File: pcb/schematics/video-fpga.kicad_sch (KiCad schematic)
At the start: 8 parts

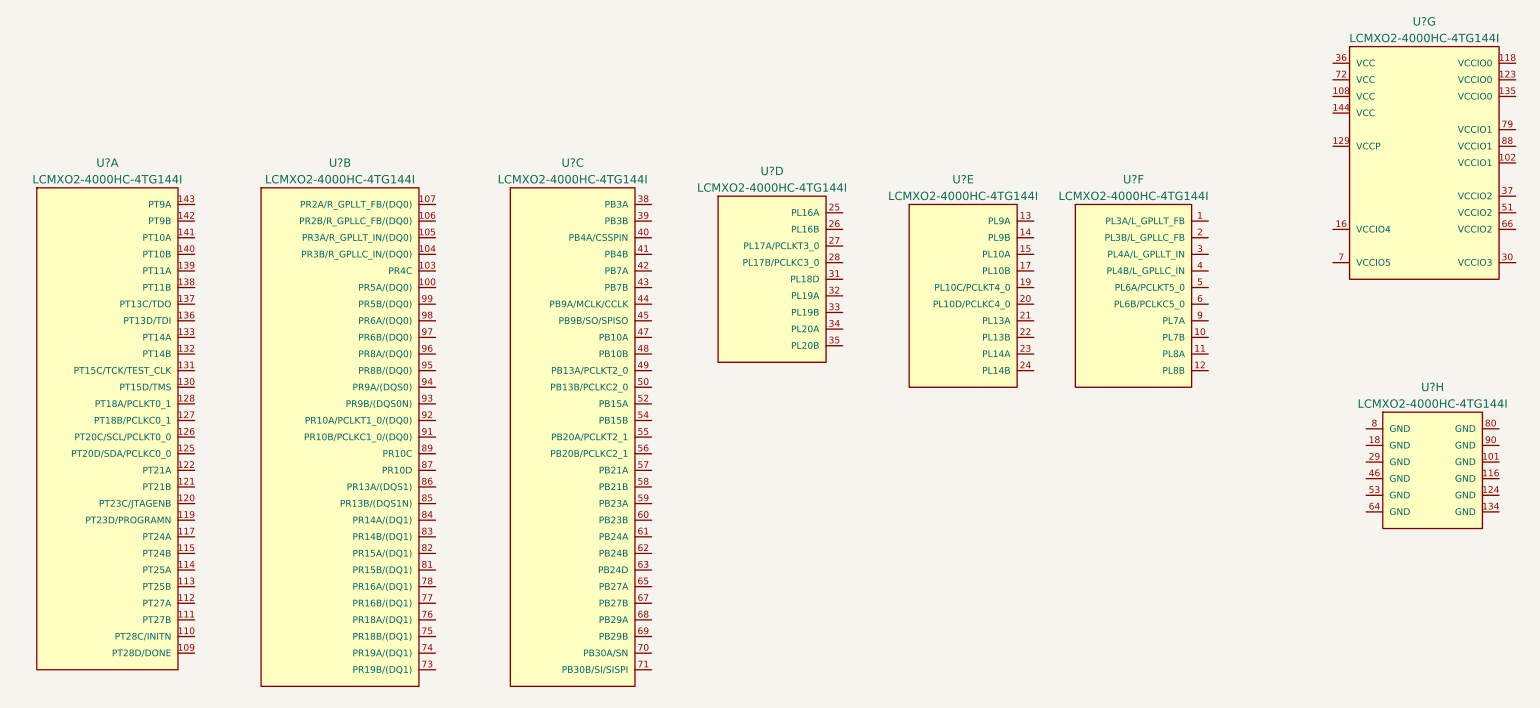
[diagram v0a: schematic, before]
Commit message: change lcmxo2-4000hc for lcmxo2-7000hc to have enough ebr for 1080p text mode
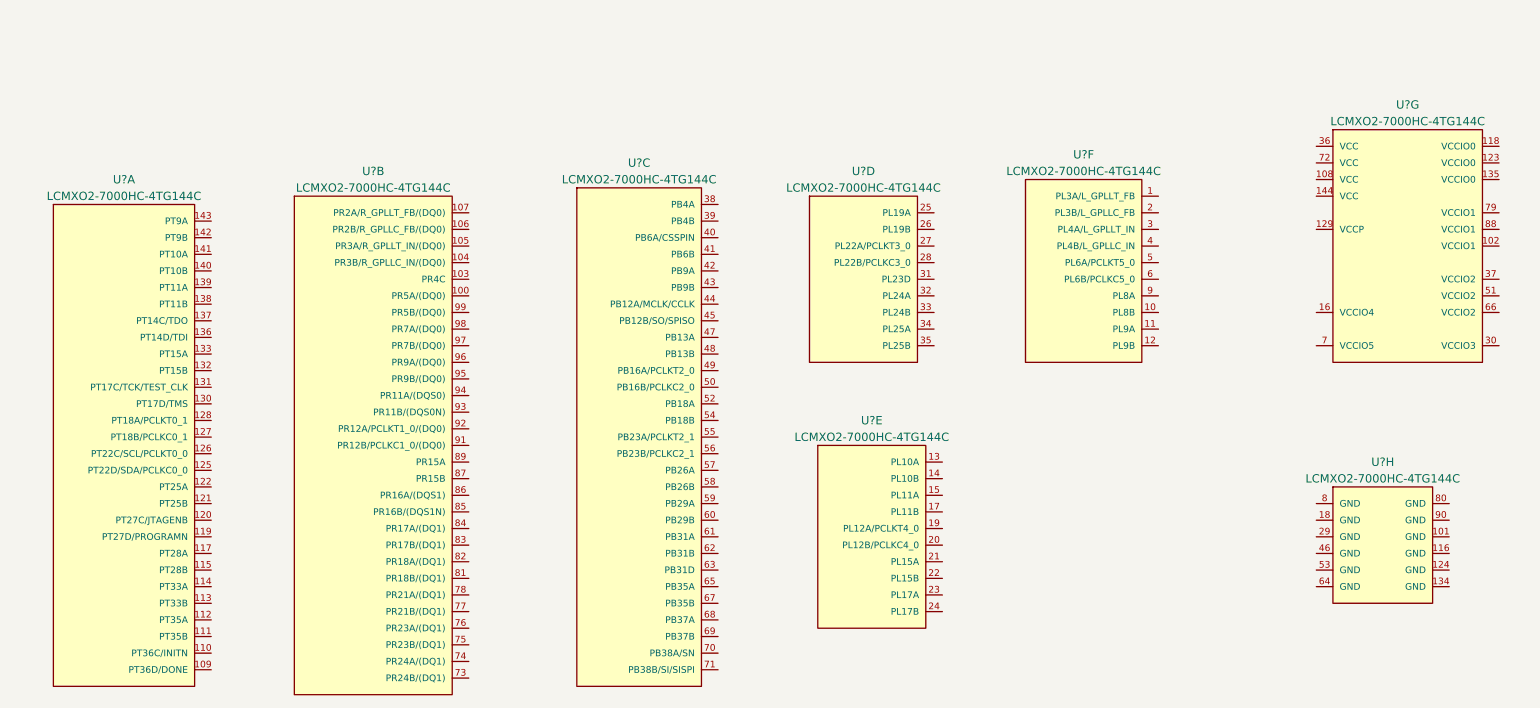
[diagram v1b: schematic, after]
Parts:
- removed U? (x8): LCMXO2-4000HC-4TG144I, Lattice_Semiconductor-LCMXO2-4000HC-4TG144I-*, symbol LCMXO2-4000HC-4TG144I:LCMXO2-4000HC-4TG144I
- added U? (x8): LCMXO2-7000HC-4TG144C, Lattice_Semiconductor-LCMXO2-7000HC-4TG144C-*, symbol LCMXO2-7000HC-4TG144C:LCMXO2-7000HC-4TG144C

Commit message: add bypass to the video controller
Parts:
- added C? (x16): 100n, symbol Device:C_Small
- added C? (x13): 10n, symbol Device:C_Small
- added C? (x7): 1u, symbol Device:C_Small
- added C? (x3): 1n, symbol Device:C_Small
- added D? (x10): D_TVS, symbol Device:D_TVS
- added J? (x2): Conn_01x06, symbol Connector_Generic:Conn_01x06
- added R? (x4): 10k, symbol Device:R_Small
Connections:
- new net +3V3: C?.1, C?.1, C?.1, C?.1, C?.1, C?.1, C?.1, C?.1, C?.1, C?.1, C?.1, C?.1, C?.1, C?.1, C?.1, C?.1, C?.1, C?.1, C?.1, C?.1, C?.1, C?.1, C?.1, C?.1, C?.1, C?.1, C?.1, C?.1, C?.1, C?.1, C?.1, C?.1, C?.1, C?.1, C?.1, C?.1, C?.1, C?.1, C?.1, D?.2 (A2), D?.2 (A2), J?.1 (Pin_1), J?.1 (Pin_1), R?.1, R?.1, R?.1, R?.1, U?.140 (PT10B), U?.141 (PT10A), U?.142 (PT9B), U?.143 (PT9A)
- new net CCK: D?.2 (A2), J?.2 (Pin_2)
- new net GND: C?.2, C?.2, C?.2, C?.2, C?.2, C?.2, C?.2, C?.2, C?.2, C?.2, C?.2, C?.2, C?.2, C?.2, C?.2, C?.2, C?.2, C?.2, C?.2, C?.2, C?.2, C?.2, C?.2, C?.2, C?.2, C?.2, C?.2, C?.2, C?.2, C?.2, C?.2, C?.2, C?.2, C?.2, C?.2, C?.2, C?.2, C?.2, C?.2, D?.1 (A1), D?.1 (A1), D?.1 (A1), D?.1 (A1), D?.1 (A1), D?.1 (A1), D?.1 (A1), D?.1 (A1), D?.1 (A1), D?.1 (A1), J?.6 (Pin_6), J?.6 (Pin_6), U?.138 (PT11B), U?.139 (PT11A), U?.140 (PT10B), U?.141 (PT10A), U?.142 (PT9B), U?.143 (PT9A)
- new net MISO: D?.2 (A2), J?.4 (Pin_4)
- new net MOSI: D?.2 (A2), J?.3 (Pin_3)
- new net SN: D?.2 (A2), J?.5 (Pin_5), R?.2
- new net TCK: D?.2 (A2), J?.2 (Pin_2)
- new net TDI: D?.2 (A2), J?.3 (Pin_3), R?.2
- new net TDO: D?.2 (A2), J?.4 (Pin_4), R?.2
- new net TMS: D?.2 (A2), J?.5 (Pin_5), R?.2
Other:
- note added: "JTAG connector"
- note added: "SPI connector"
- moved on the sheet: U?A

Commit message: add jtag signals to the video controller
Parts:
- added C?: 100p, symbol Device:C_Small
- added R?: 10k, symbol Device:R_Small
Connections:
- net CCK: now also U?.137 (PT14C/TDO)
- net GND: now also C?.2
- net MISO: now also U?.136 (PT14D/TDI)
- net SN: now also U?.109 (PT36D/DONE)
- net TCK: now also U?.131 (PT17C/TCK/TEST_CLK), R?.1
- net TDI: now also U?.136 (PT14D/TDI)
- net TDO: now also U?.137 (PT14C/TDO)
- net TMS: now also U?.130 (PT17D/TMS)
- new net: C?.1, R?.2
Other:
- moved on the sheet: D?, U?A

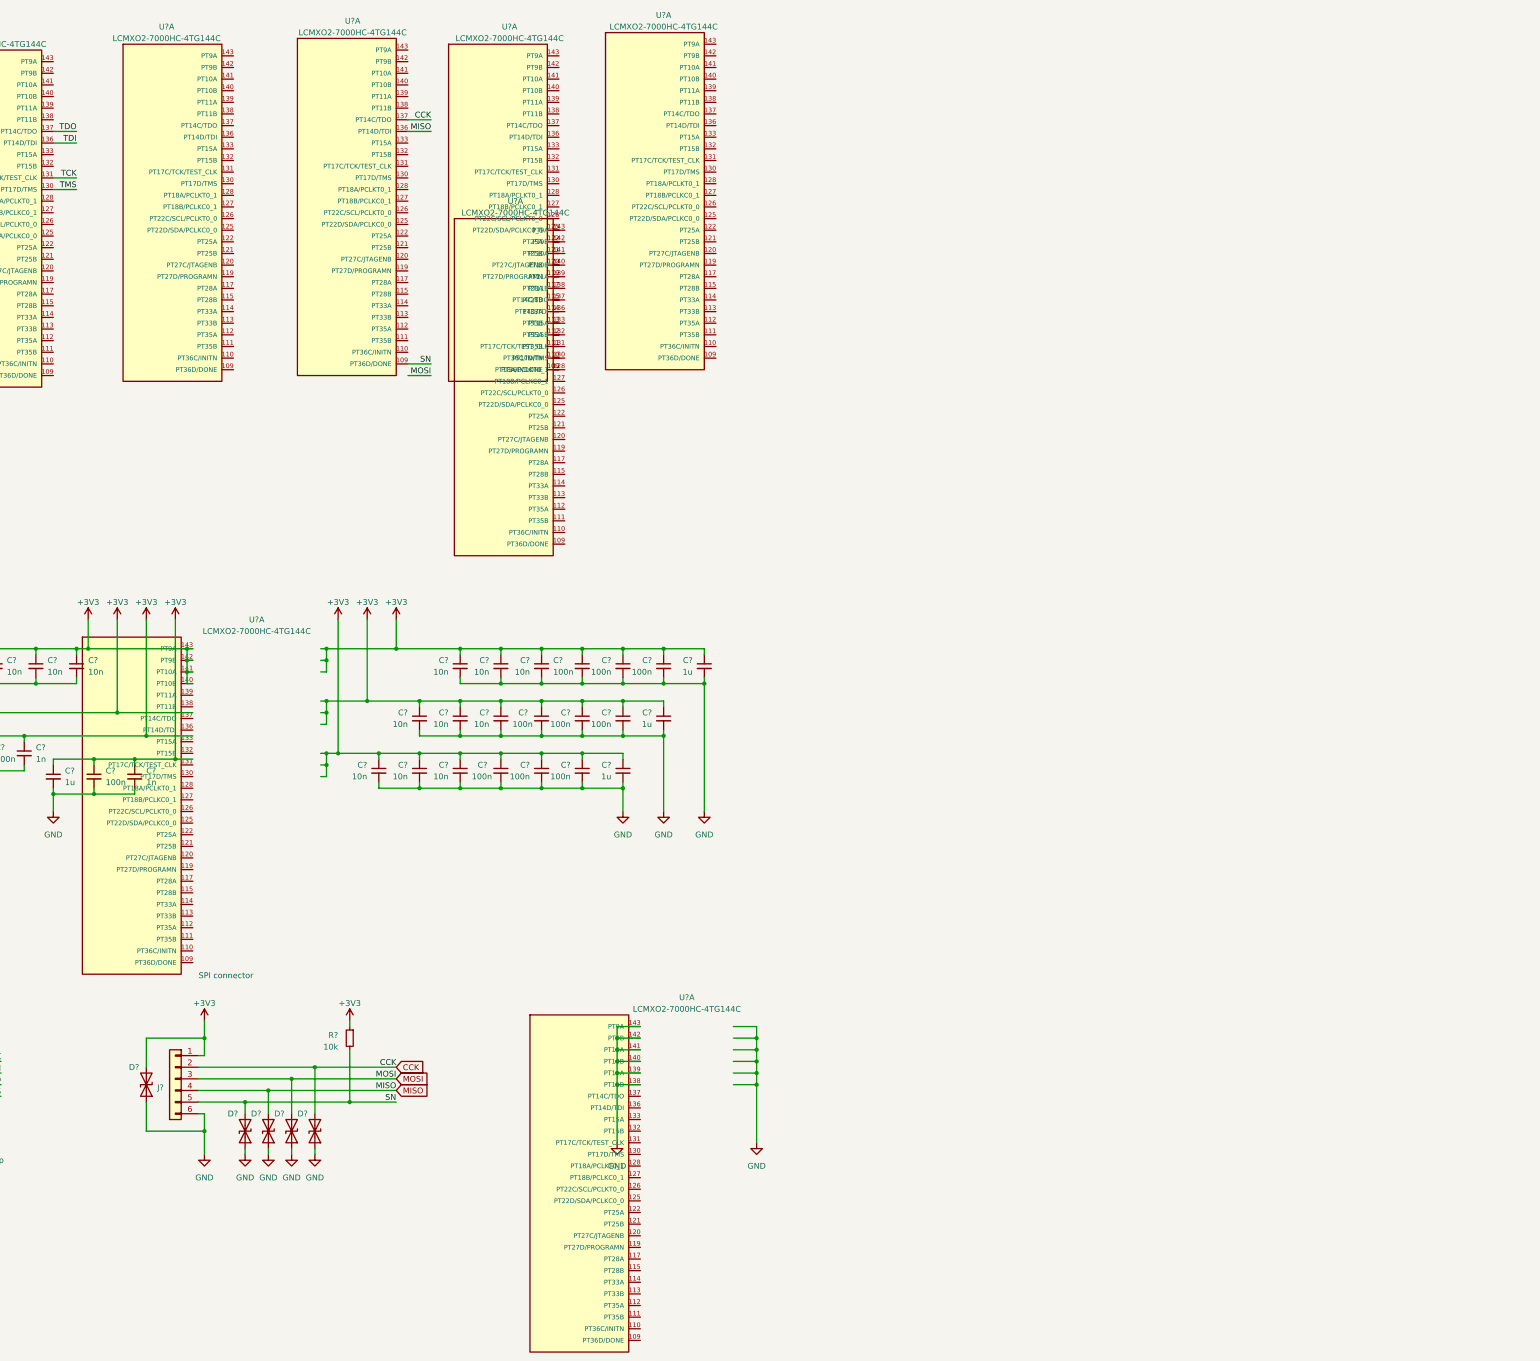
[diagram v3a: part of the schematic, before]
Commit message: add i2c mux for ddc
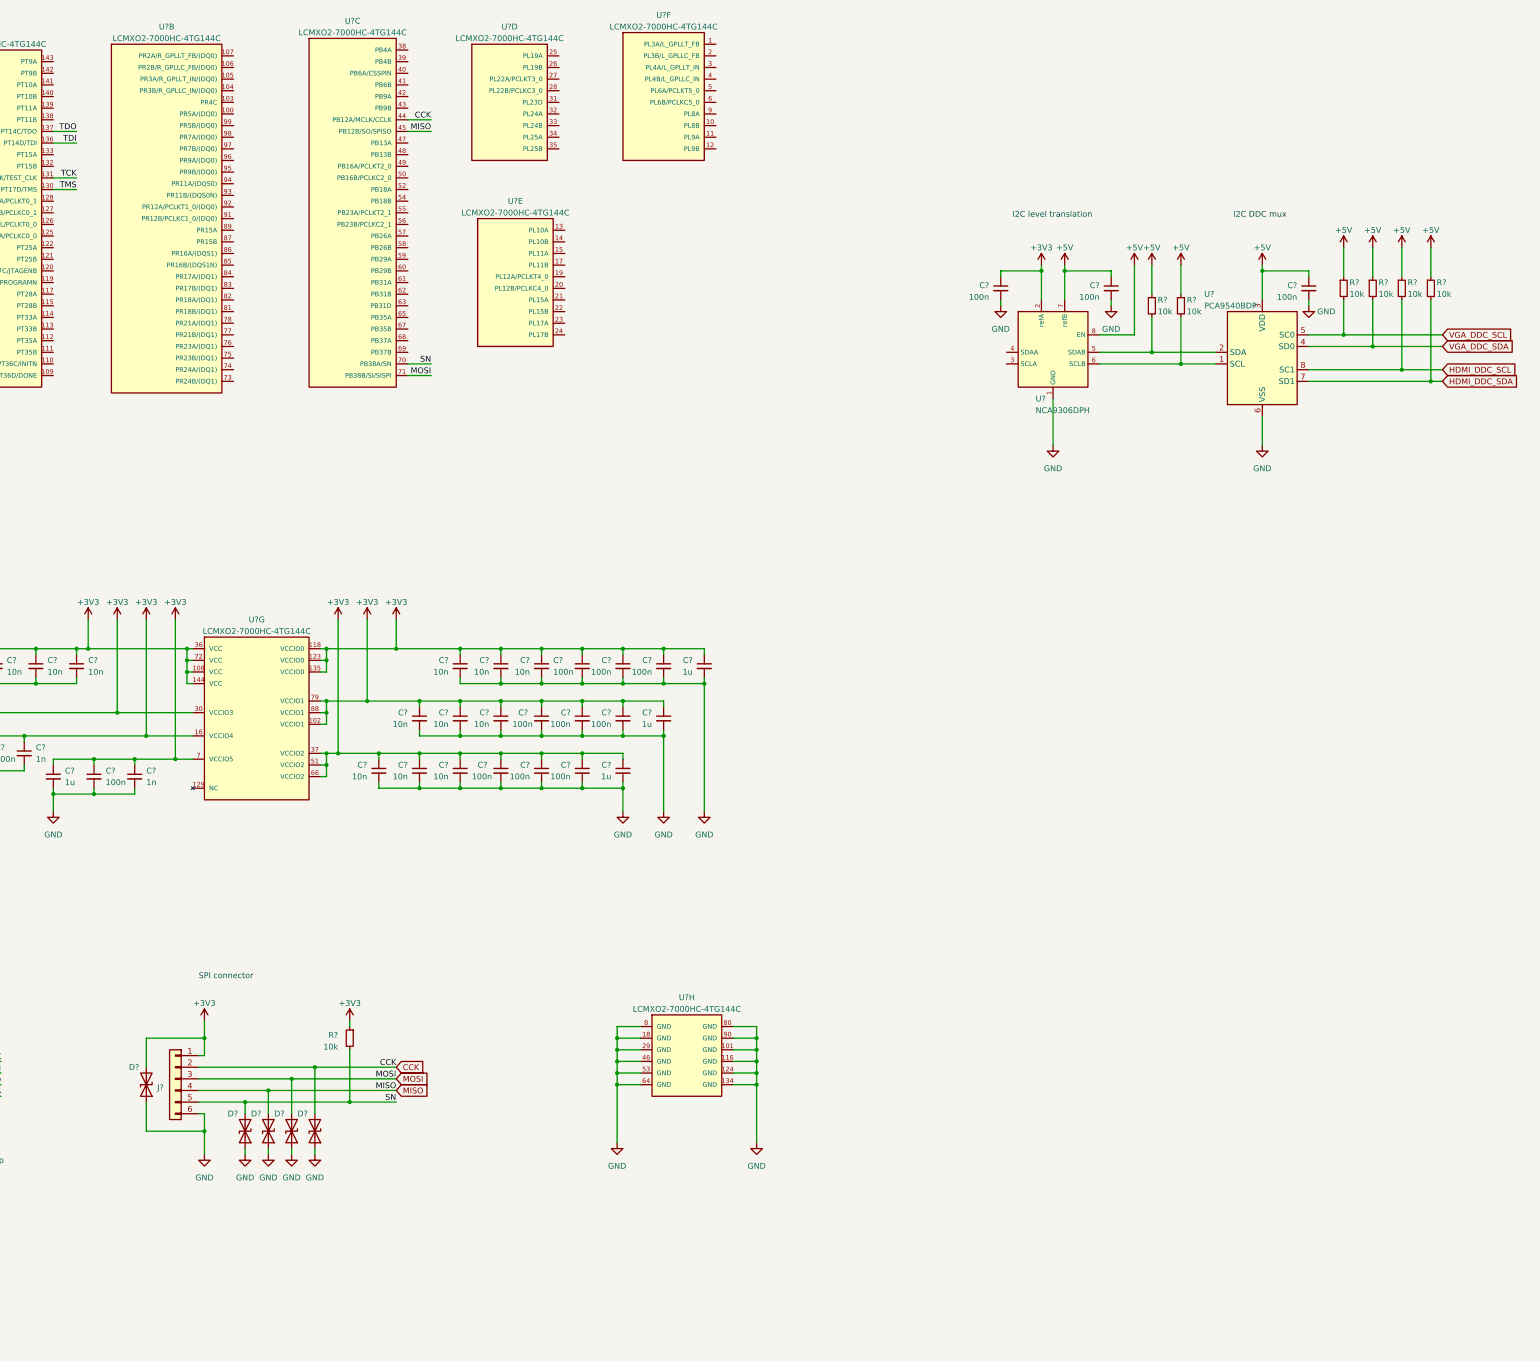
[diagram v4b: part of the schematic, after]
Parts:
- added C? (x3): 100n, symbol Device:C_Small
- added R? (x6): 10k, symbol Device:R_Small
- added U?: NCA9306DPH, symbol NCA9306:NCA9306DPH
- added U?: PCA9540BDP, symbol PCA9540:PCA9540BDP
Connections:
- net +3V3: now also U?.102 (VCCIO1), U?.108 (VCC), U?.118 (VCCIO0), U?.123 (VCCIO0), U?.135 (VCCIO0), U?.144 (VCC), U?.16 (VCCIO4), U?.30 (VCCIO3), U?.36 (VCC), U?.37 (VCCIO2), U?.51 (VCCIO2), U?.66 (VCCIO2), U?.7 (VCCIO5), U?.72 (VCC), U?.79 (VCCIO1), U?.88 (VCCIO1), C?.1, U?.2 (refA); no longer U?.140 (PT10B), U?.141 (PT10A), U?.142 (PT9B), U?.143 (PT9A)
- net CCK: now also U?.44 (PB12A/MCLK/CCLK); no longer U?.137 (PT14C/TDO)
- net GND: now also U?.101 (GND), U?.116 (GND), U?.124 (GND), U?.134 (GND), U?.18 (GND), U?.29 (GND), U?.46 (GND), U?.53 (GND), U?.64 (GND), U?.8 (GND), U?.80 (GND), U?.90 (GND), C?.2, C?.2, C?.2, U?.1 (GND), U?.6 (VSS); no longer U?.138 (PT11B), U?.139 (PT11A), U?.140 (PT10B), U?.141 (PT10A), U?.142 (PT9B), U?.143 (PT9A)
- net MISO: now also U?.45 (PB12B/SO/SPISO); no longer U?.136 (PT14D/TDI)
- net MOSI: now also U?.71 (PB38B/SI/SISPI)
- net SN: now also U?.70 (PB38A/SN); no longer U?.109 (PT36D/DONE)
- new net: R?.2, U?.1 (SCL), U?.6 (SCLB)
- new net: R?.2, U?.2 (SDA), U?.5 (SDAB)
- new net +5V: C?.1, C?.1, R?.1, R?.1, R?.1, R?.1, R?.1, R?.1, U?.3 (VDD), U?.7 (refB), U?.8 (EN)
- new net HDMI_DDC_SCL: R?.2, U?.8 (SC1)
- new net HDMI_DDC_SDA: R?.2, U?.7 (SD1)
- new net VGA_DDC_SCL: R?.2, U?.5 (SC0)
- new net VGA_DDC_SDA: R?.2, U?.4 (SD0)
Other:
- note added: "I2C DDC mux"
- note added: "I2C level translation"

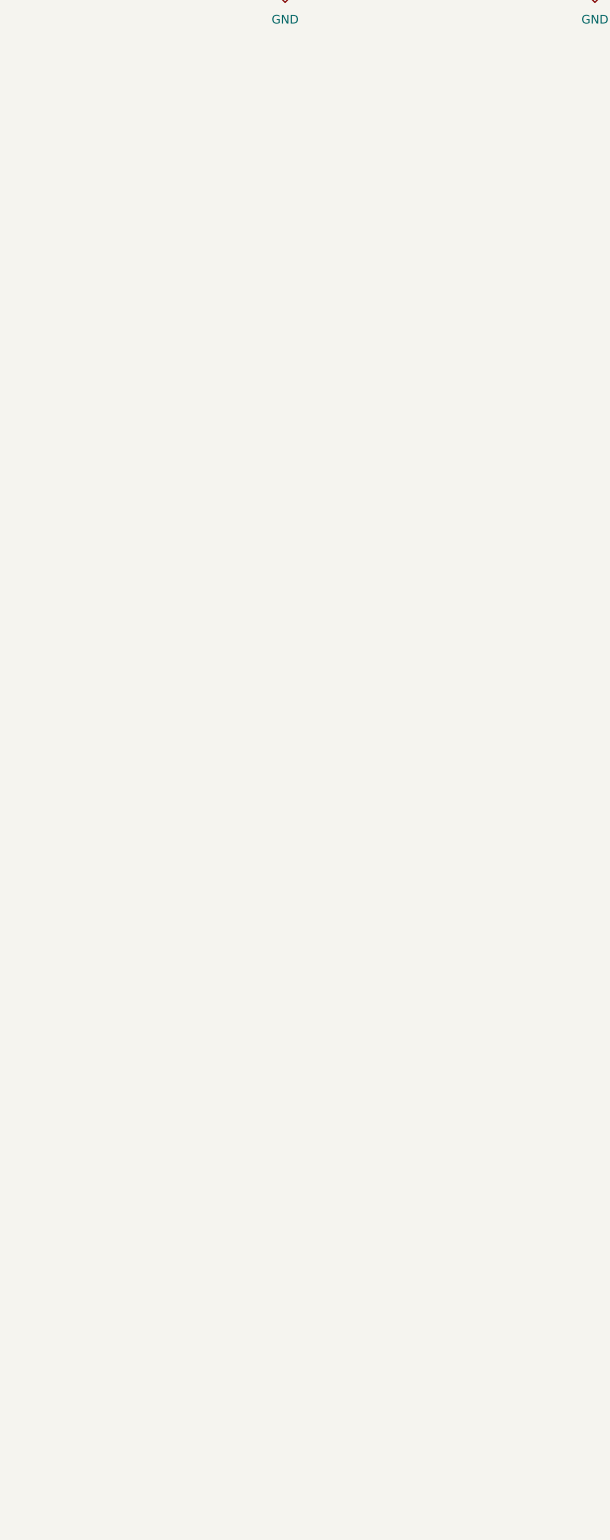
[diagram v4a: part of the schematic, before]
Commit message: add global symbals to the video controller
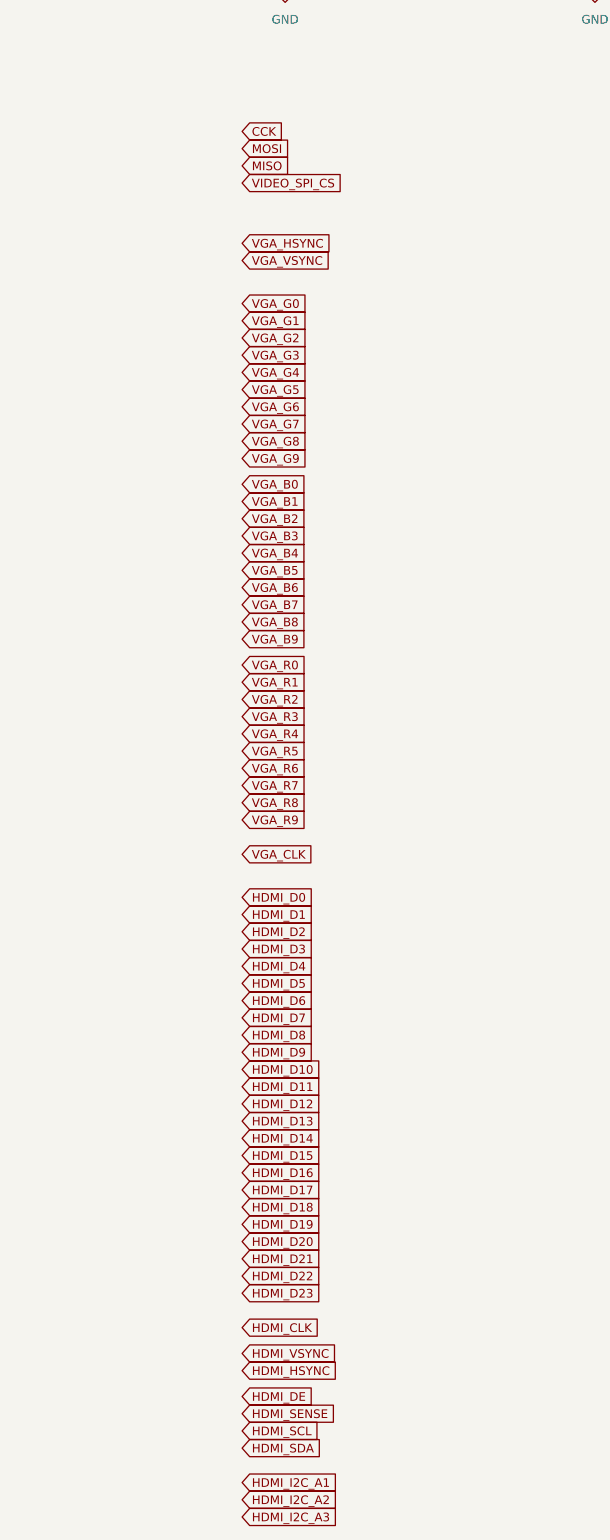
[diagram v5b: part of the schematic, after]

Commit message: moved i2c mux to another page
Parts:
- removed C? (x3): 100n, symbol Device:C_Small
- removed R? (x6): 10k, symbol Device:R_Small
- removed U?: NCA9306DPH, symbol NCA9306:NCA9306DPH
- removed U?: PCA9540BDP, symbol PCA9540:PCA9540BDP
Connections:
- net FPGA_SDA: now reaches U?.125 (PT22D/SDA/PCLKC0_0)
- net FPGA_SCL: now reaches U?.126 (PT22C/SCL/PCLKT0_0)
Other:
- note removed: "I2C DDC mux"
- note removed: "I2C level translation"
- moved on the sheet: C?, D?, J?, R?, U?A, U?B, U?C, U?D, U?E, U?F, U?G, U?H

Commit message: choose components and add footprints
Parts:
- C33, C48, C55, C56, C59, C68, C69: renamed from C?; footprint (none) -> Capacitor_SMD:C_0805_2012Metric; Part Number (none) -> 885012207022
- C34, C35, C36, C37, C45, C46, C47, C52, C53, C54, C57, C60, C65, C66, C67, C70: renamed from C?; footprint (none) -> Capacitor_SMD:C_0603_1608Metric; Part Number (none) -> EMK107B7104KA-T
- C38, C39, C40, C41, C42, C43, C44, C49, C50, C51, C62, C63, C64: renamed from C?; footprint (none) -> Capacitor_SMD:C_0402_1005Metric; Part Number (none) -> C0402C103K5RAC7411
- C58, C61, C71: renamed from C?; footprint (none) -> Capacitor_SMD:C_0402_1005Metric; Part Number (none) -> GRM155R70J102KA01D
- C72: renamed from C?; footprint (none) -> Capacitor_SMD:C_0402_1005Metric; Part Number (none) -> C0402C101J5RACTU
- D11, D12, D13, D14, D15, D16, D17, D18, D19, D20: renamed from D?; footprint (none) -> Diode_SMD:D_0603_1608Metric; Part Number (none) -> 82356240030
- J5, J6: renamed from J?; footprint (none) -> Connector:Tag-Connect_TC2030-IDC-FP_2x03_P1.27mm_Vertical
- R10, R11, R7, R8, R9: renamed from R?; footprint (none) -> Resistor_SMD:R_0603_1608Metric; Part Number (none) -> RC0603JR-0710KL
- U4: renamed from U?; footprint Lattice_Semiconductor-LCMXO2-7000HC-4TG144C-* -> LCMXO2-7000HC-4TG144C:Lattice_Semiconductor-LCMXO2-7000HC-4TG144C-Level_C; Part Number (none) -> LCMXO2-7000HC-4TG144C
